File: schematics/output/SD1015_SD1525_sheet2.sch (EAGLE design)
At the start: 263 parts, among them U1A U1 section, pins 1/2/3 - DIFF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, U1B U1 section, pins 4/5/6/7/8, U2B U2 section - A.V. AMPLIFIER, U9B U9 section - ECC

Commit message: Take pin positions from the traced wires, removing the bends
Every bend you could see was a pin drawn where the traced wire did not expect
it, and the reconciliation step dutifully adding an elbow to bridge the gap.
Measured against the tracing: PWM and LOCK-OUT pins were about 4 mm out
vertically, the DRIVERs 8 mm horizontally, the transformer primaries 10-13 mm.

A run already records both its endpoint and the pin that endpoint lands on, so
each pin's offset from its part's centre was in the data all along -- no new
transcription needed. derive_pin_offsets() reads it out and the size-variable
symbols use it. Spacing a block's pins evenly was a guess, and the drawing does
not space them evenly.

Only the offset across the wire is applied. Along the wire it is just a longer
lead, so resistors and op-amps keep their standard proportions rather than
being stretched to match the tracing.

That left sub-millimetre steps, which turned out to be ScanPlacer rounding part
positions onto a 2.54 mm grid: a pin derived from the same pixels as its wire
cannot line up if one of them is then rounded and the other is not. Scan
placement no longer snaps, and uses the fixed SCAN mm_per_px scale so the pin
derivation and the wire mapping are the same linear map.

Transcribed runs: 63 wire segments down to 30, with 11 of the 15 nets now a
single straight wire. CLOCK's remains a single bend, which is what the drawing
draws.

Netlist untouched, all 15 nets still drawn, 173 -> 177 tests.

Co-Authored-By: Claude Opus 5 <noreply@anthropic.com>
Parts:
- C61: device sd1525:DS_CPOL_1 -> sd1525:DS_CPOL_2
- DRIVER2: device sd1525:DS_BLOCK_6 -> sd1525:DS_BLOCK_7
- FGF: device sd1525:DS_BLOCK_8 -> sd1525:DS_BLOCK_9
- R104: device sd1525:DS_R_1 -> sd1525:DS_R_3
- R137, R94, R95: device sd1525:DS_R_1 -> sd1525:DS_R_2
- R73, R76: device sd1525:DS_R_1 -> sd1525:DS_R_4
- SURGE_DETECTOR: device sd1525:DS_BLOCK_7 -> sd1525:DS_BLOCK_8
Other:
- moved on the sheet: C61, CLOCK, DRIVER1, DRIVER2, LOCKOUT, PWM, R104, R137, R73, R76, R95, U9A

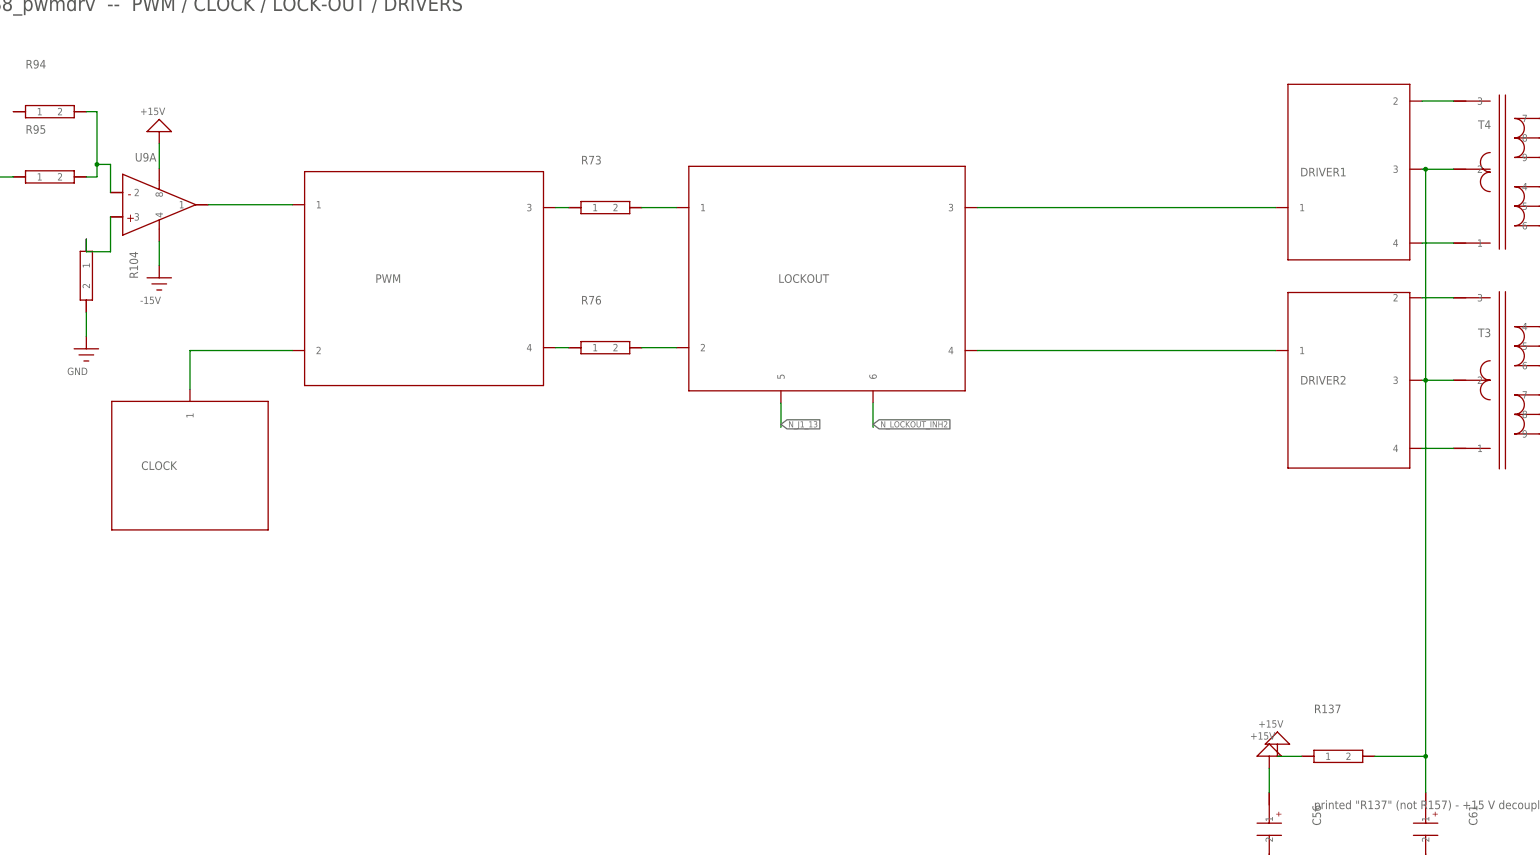
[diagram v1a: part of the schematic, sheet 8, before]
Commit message: Put block and amplifier pins where the drawing puts them, and merge rail symbols
Four problems reported off the Fusion render, three of them one cause.

Block pins sat 2.54 mm outside the box edge, where the drawing attaches its
wires at the edge itself. That shrank every gap around a series part -- R73 had
2.74 mm to PWM and 7.24 mm to LOCK-OUT -- and it pushed DRIVER pin 3 to within
0.76 mm of the centre-tap spine, so the junction dot landed on top of the pin
and the connection read as ambiguous. Block pins now take their traced position
on both axes: 9.20 mm of clear stub to the spine.

The amplifier had the same fault and worse. U9's inputs were drawn 7 mm from
where its wires arrive, so R104's wire ran down past its own pin and doubled
back up to reach it. The triangle is now built from the traced pin positions,
and that wire is a plain two-segment elbow.

Series parts are centred between the pins they join. The drawing's own spacing
is uneven and a fixed-size symbol in a gap that is not its own width exaggerates
it; R73 and R76 now sit 7.58 mm from each neighbour.

Rail pins closer than 12.7 mm share one symbol wired between them. The drawing
brings +15 V down to a node and fans out; a symbol per pin stacked two on top of
each other and read as two separate supplies. The joining wires are real wires
and take the same no-overlap rule -- one GND cluster on S1_input would have lain
along another net, so those pins stay separate.

Traced sizes and pin positions are now correctly confined to the scan layout.
They had leaked into the auto-placed sheets, where they only make symbols too
big for the grid; the symbol-collision test caught it.

Netlist untouched, all 15 nets still drawn, zero overlapping wires, 177 -> 182
tests.

Co-Authored-By: Claude Opus 5 <noreply@anthropic.com>
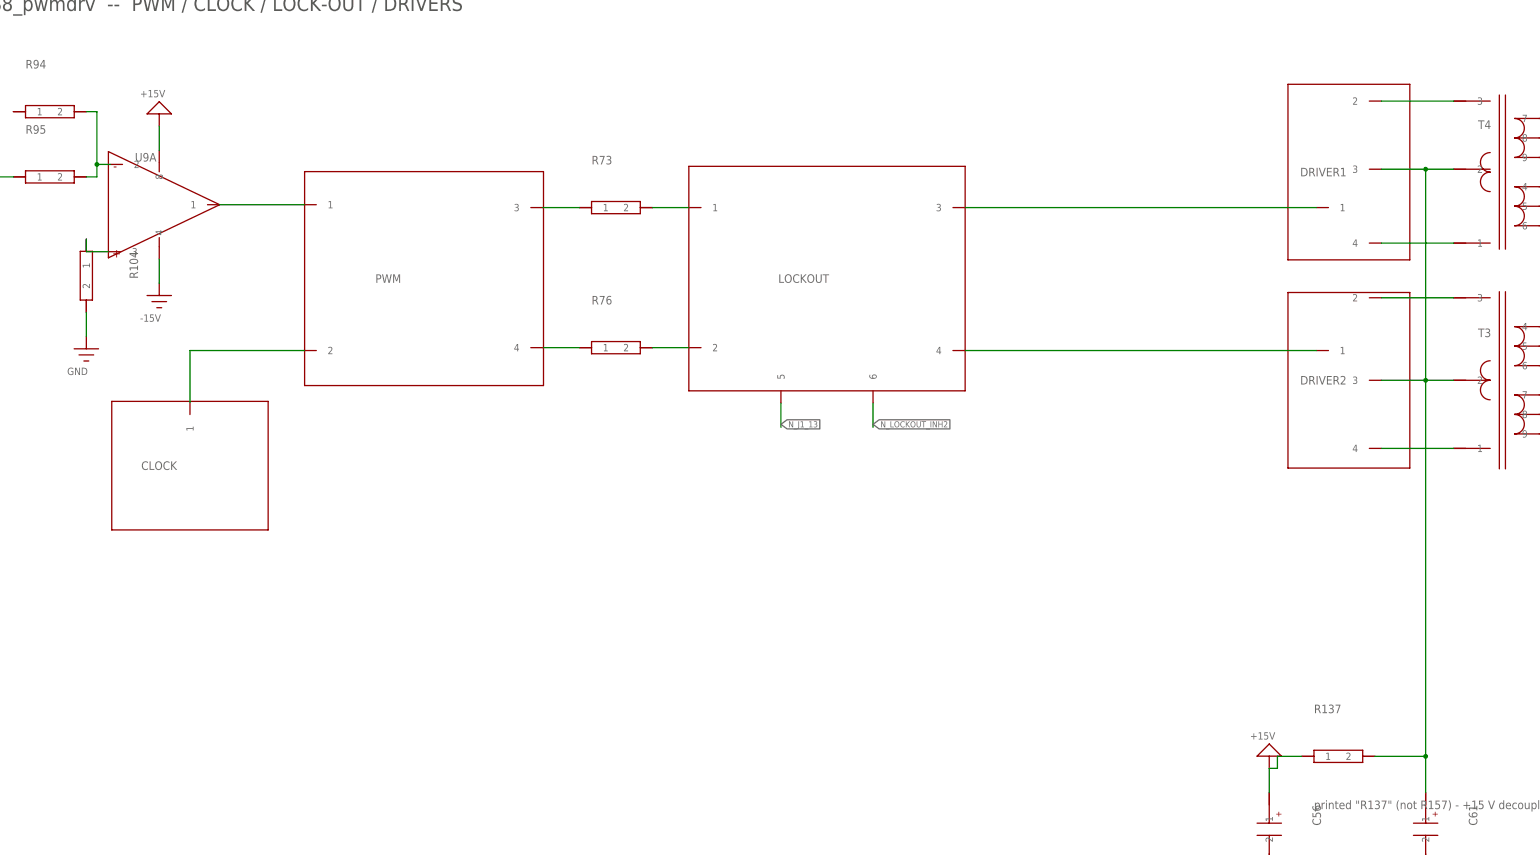
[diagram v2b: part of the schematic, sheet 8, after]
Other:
- moved on the sheet: CLOCK, R73, R76
